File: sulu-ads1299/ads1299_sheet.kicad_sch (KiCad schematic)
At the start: 13 parts

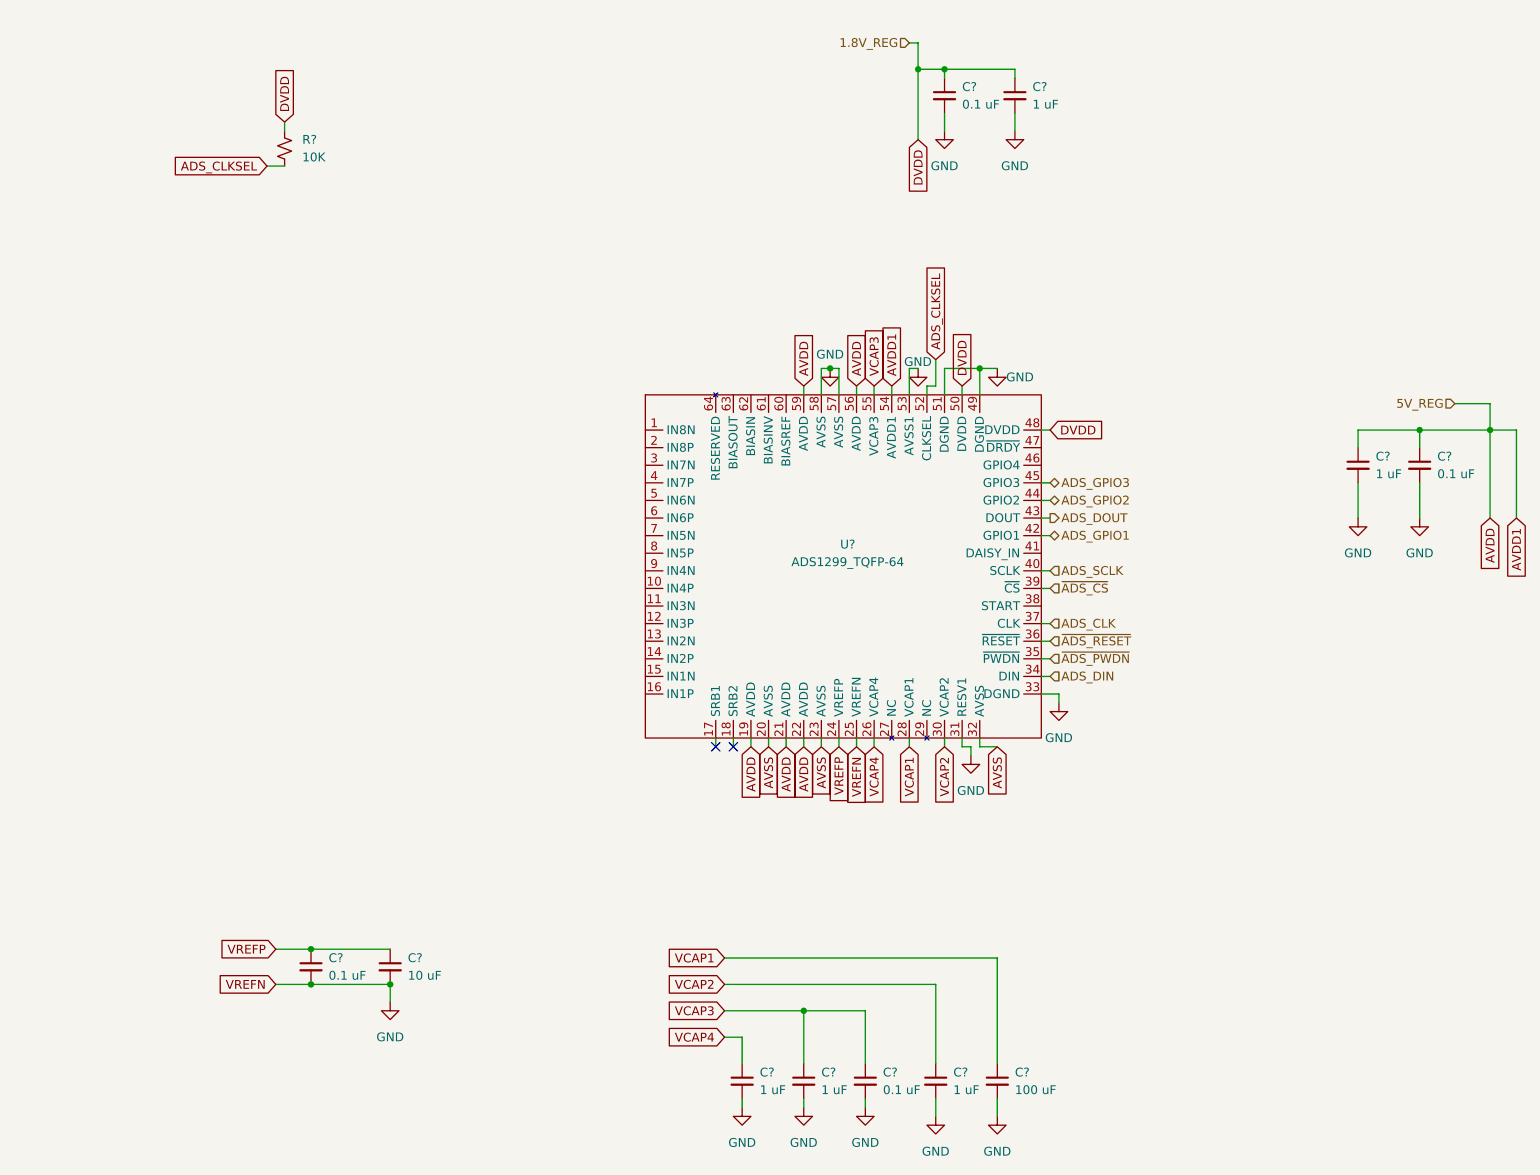
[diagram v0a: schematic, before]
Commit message: Sulu-ads1299 schematic largely completed
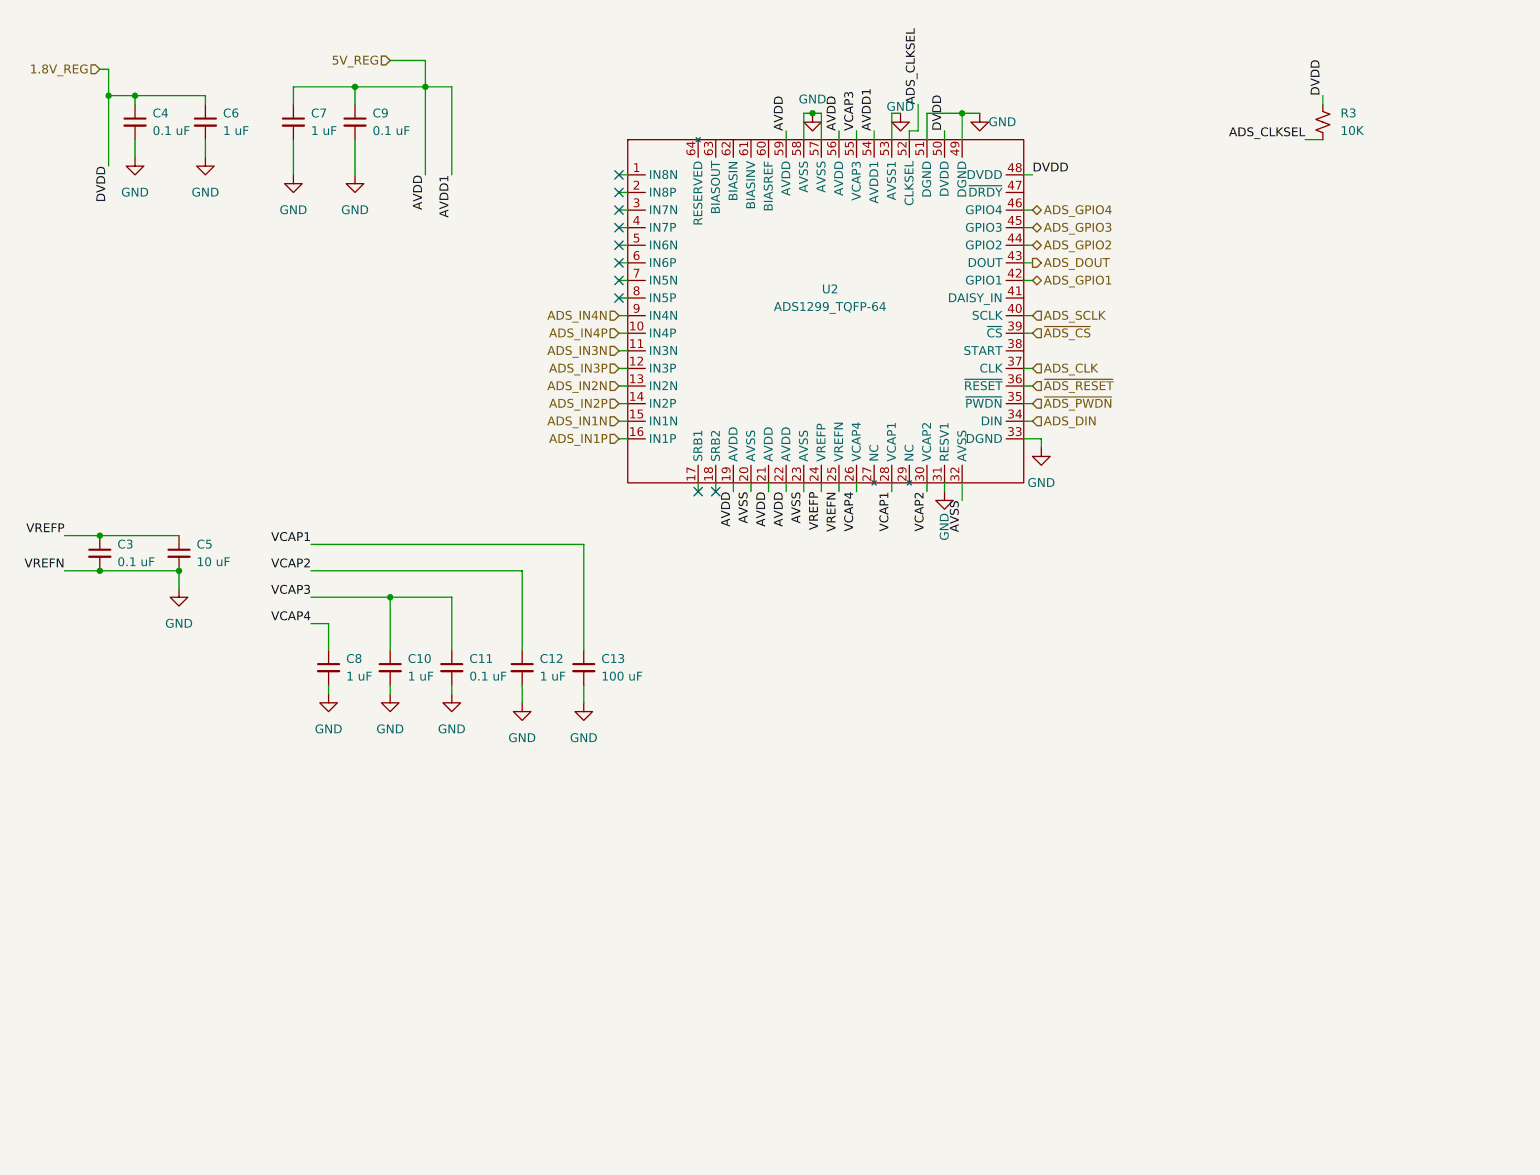
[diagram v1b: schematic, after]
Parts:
- gave numbers to parts that had none: 13
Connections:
- net ADS_IN4P: now reaches U2.10 (IN4P)
- net ADS_IN3N: now reaches U2.11 (IN3N)
- net ADS_IN3P: now reaches U2.12 (IN3P)
- net ADS_IN2N: now reaches U2.13 (IN2N)
- net ADS_IN2P: now reaches U2.14 (IN2P)
- net ADS_IN1N: now reaches U2.15 (IN1N)
- net ADS_IN1P: now reaches U2.16 (IN1P)
- net ADS_GPIO4: now reaches U2.46 (GPIO4)
- net ADS_IN4N: now reaches U2.9 (IN4N)
- net AVDD renamed 5V_REG
- net DVDD renamed 1.8V_REG
- no-connect marks 2 -> 10
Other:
- moved on the sheet: C10, C11, C12, C13, C3, C4, C5, C6, C7, C8, C9, R3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

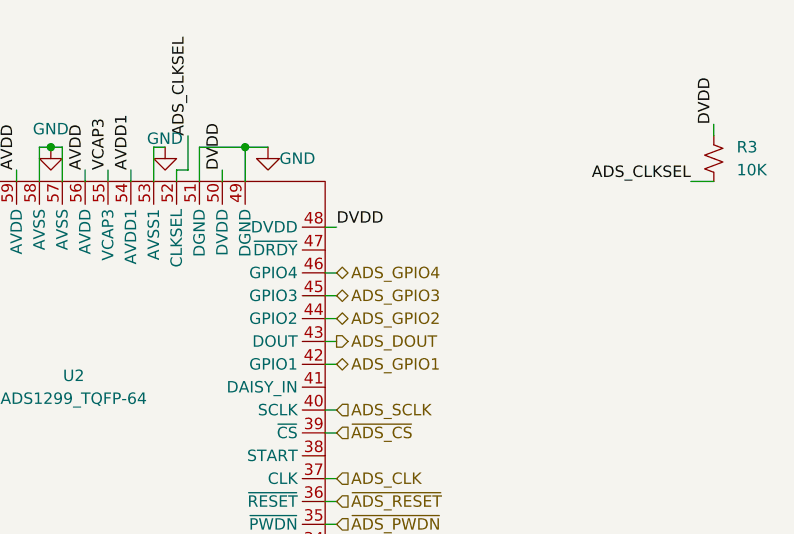
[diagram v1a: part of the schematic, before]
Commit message: Sulu-ads1299 migrating libs and fixing ERC
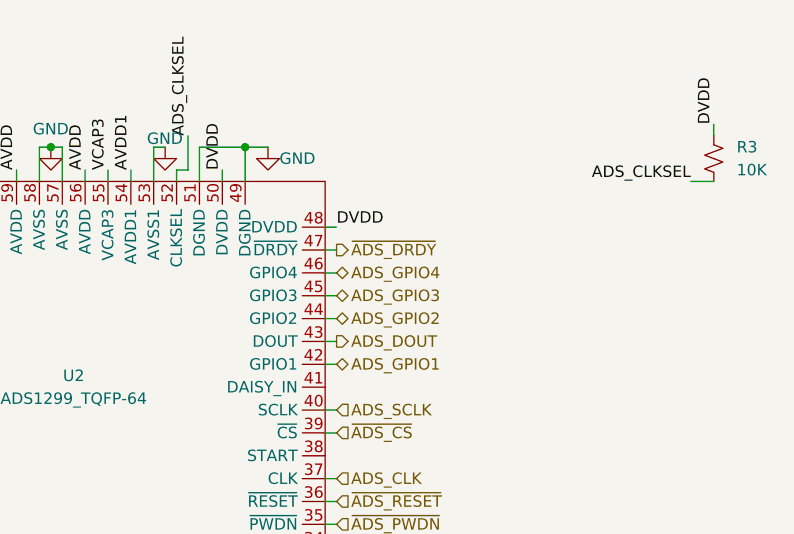
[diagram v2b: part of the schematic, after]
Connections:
- net ~{ADS_DRDY}: now reaches U2.47 (~{DRDY})
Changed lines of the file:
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@@
+    (stroke (width 0) (type default) (color 0 0 0 0))
+  )
+  (wire (pts (xy 162.56 43.18) (xy 163.83 43.18))
     (stroke (width 0) (type default) (color 0 0 0 0))
   )
@@
     (effects (font (size 1.27 1.27)) (justify left))
   )
+  (hierarchical_label "~{ADS_DRDY}" (shape output) (at 163.83 43.18 0)
+    (effects (font (size 1.27 1.27)) (justify left))
+  )

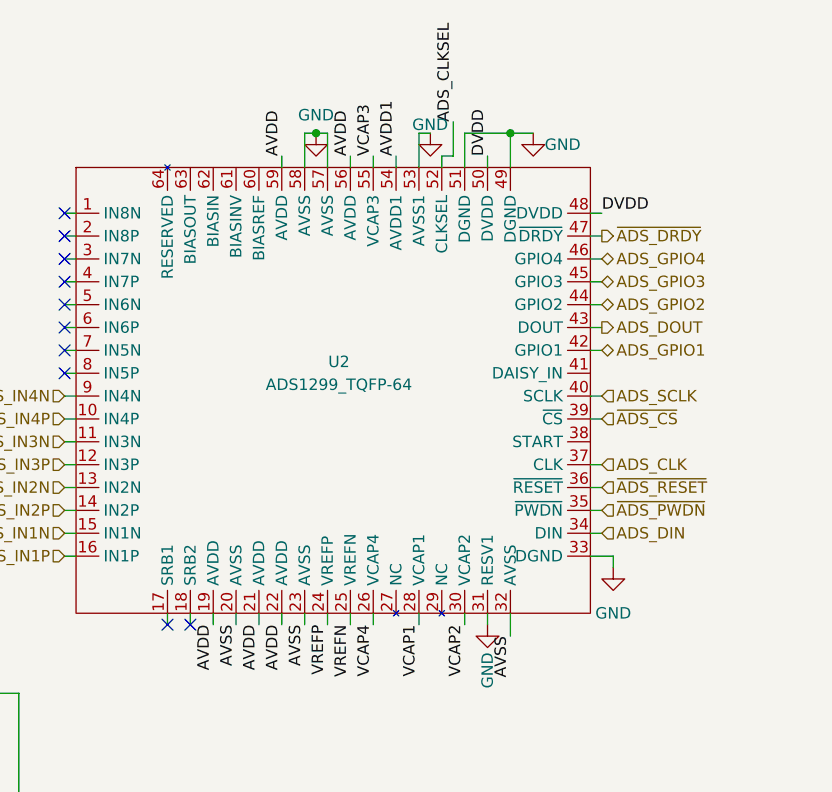
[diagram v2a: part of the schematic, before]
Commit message: Sulu-ads1299 started layout & imported shared footprints
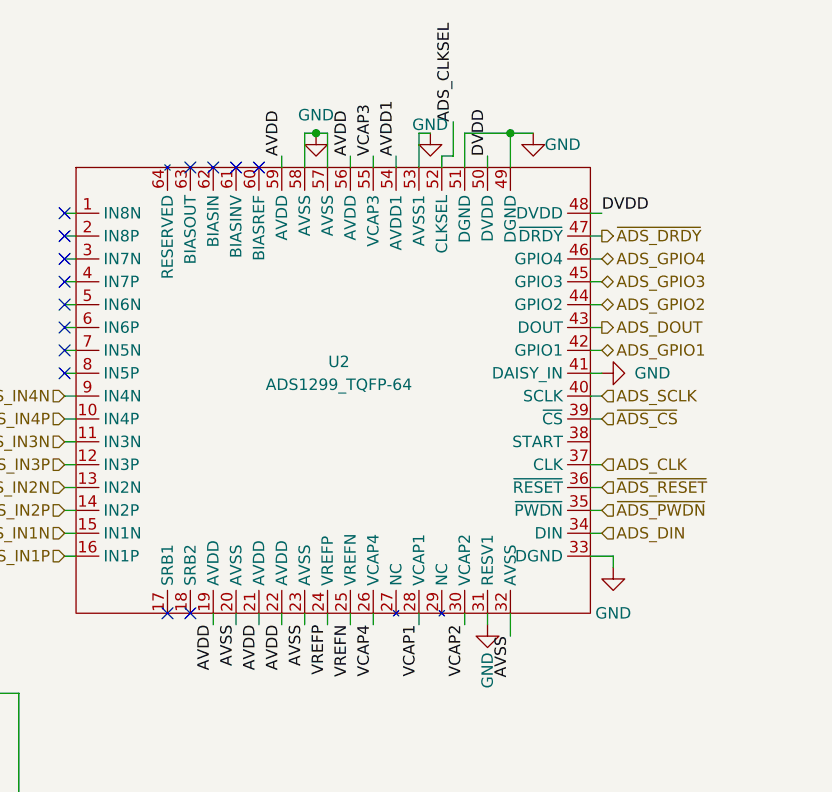
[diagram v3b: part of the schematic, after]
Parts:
- C10, C11, C3, C4, C5, C6, C7, C8, C9: footprint (none) -> Capacitor_SMD:C_0402_1005Metric
- R3: footprint (none) -> Resistor_SMD:R_0402_1005Metric
- U2: footprint (none) -> Package_QFP:TQFP-64_10x10mm_P0.5mm
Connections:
- net GND: now also U2.41 (DAISY_IN)
- no-connect marks 10 -> 14
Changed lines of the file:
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@@
   )
   (no_connect (at 104.14 48.26))
+  (no_connect (at 123.19 35.56))
+  (no_connect (at 118.11 85.09))
   (no_connect (at 104.14 40.64))
-  (no_connect (at 115.57 86.36))
+  (no_connect (at 120.65 35.56))
   (no_connect (at 104.14 50.8))
   (no_connect (at 104.14 45.72))
@@
   (no_connect (at 104.14 58.42))
   (no_connect (at 104.14 55.88))
-  (no_connect (at 118.11 86.36))
+  (no_connect (at 115.57 85.09))
+  (no_connect (at 118.11 35.56))
+  (no_connect (at 125.73 35.56))
   (no_connect (at 104.14 53.34))
   (wire (pts (xy 29.21 97.79) (xy 40.64 97.79))
@@
     (stroke (width 0) (type default) (color 0 0 0 0))
   )
-  (wire (pts (xy 115.57 86.36) (xy 115.57 85.09))
-    (stroke (width 0) (type default) (color 0 0 0 0))
-  )
   (wire (pts (xy 138.43 34.29) (xy 138.43 35.56))
     (stroke (width 0) (type default) (color 0 0 0 0))
@@
     (stroke (width 0) (type default) (color 0 0 0 0))
   )
+  (wire (pts (xy 162.56 58.42) (xy 163.83 58.42))
+    (stroke (width 0) (type default) (color 0 0 0 0))
+  )
   (wire (pts (xy 162.56 76.2) (xy 163.83 76.2))
     (stroke (width 0) (type default) (color 0 0 0 0))
@@
   )
   (wire (pts (xy 66.04 27.94) (xy 57.15 27.94))
-    (stroke (width 0) (type default) (color 0 0 0 0))
-  )
-  (wire (pts (xy 118.11 85.09) (xy 118.11 86.36))
     (stroke (width 0) (type default) (color 0 0 0 0))
   )
@@
       (effects (font (size 1.27 1.27)) (justify left))
     )
-    (property "Footprint" "" (id 2) (at 40.64 95.25 0)
+    (property "Footprint" "Capacitor_SMD:C_0402_1005Metric" (id 2) (at 40.64 95.25 0)
       (effects (font (size 1.27 1.27)) hide)
     )
@@
     (property "Reference" "U2" (id 0) (at 134.62 57.15 0))
     (property "Value" "ADS1299_TQFP-64" (id 1) (at 134.62 59.69 0))
-    (property "Footprint" "" (id 2) (at 77.47 54.61 0)
+    (property "Footprint" "Package_QFP:TQFP-64_10x10mm_P0.5mm" (id 2) (at 77.47 54.61 0)
       (effects (font (size 1.27 1.27)) hide)
     )
@@
       (effects (font (size 1.27 1.27)) (justify left))
     )
-    (property "Footprint" "" (id 2) (at 57.15 33.02 0)
+    (property "Footprint" "Capacitor_SMD:C_0402_1005Metric" (id 2) (at 57.15 33.02 0)
       (effects (font (size 1.27 1.27)) hide)
     )
@@
       (effects (font (size 1.27 1.27)) (justify left))
     )
-    (property "Footprint" "" (id 2) (at 44.45 33.02 0)
+    (property "Footprint" "Capacitor_SMD:C_0402_1005Metric" (id 2) (at 44.45 33.02 0)
       (effects (font (size 1.27 1.27)) hide)
     )
@@
       (effects (font (size 1.27 1.27)) (justify left))
     )
-    (property "Footprint" "" (id 2) (at 62.23 111.76 0)
+    (property "Footprint" "Capacitor_SMD:C_0402_1005Metric" (id 2) (at 62.23 111.76 0)
       (effects (font (size 1.27 1.27)) hide)
     )
@@
       (effects (font (size 1.27 1.27)) (justify left))
     )
-    (property "Footprint" "" (id 2) (at 66.04 33.02 0)
+    (property "Footprint" "Capacitor_SMD:C_0402_1005Metric" (id 2) (at 66.04 33.02 0)
       (effects (font (size 1.27 1.27)) hide)
     )
@@
       (effects (font (size 1.27 1.27)) (justify left))
     )
-    (property "Footprint" "" (id 2) (at 29.21 95.25 0)
+    (property "Footprint" "Capacitor_SMD:C_0402_1005Metric" (id 2) (at 29.21 95.25 0)
       (effects (font (size 1.27 1.27)) hide)
     )
@@
       (effects (font (size 1.27 1.27)) (justify left))
     )
-    (property "Footprint" "" (id 2) (at 71.12 111.76 0)
+    (property "Footprint" "Capacitor_SMD:C_0402_1005Metric" (id 2) (at 71.12 111.76 0)
       (effects (font (size 1.27 1.27)) hide)
     )
@@
       (effects (font (size 1.27 1.27)) (justify left))
     )
-    (property "Footprint" "" (id 2) (at 205.74 33.02 0)
+    (property "Footprint" "Resistor_SMD:R_0402_1005Metric" (id 2) (at 205.74 33.02 0)
       (effects (font (size 1.27 1.27)) hide)
     )
@@
       (effects (font (size 1.27 1.27)) (justify left))
     )
-    (property "Footprint" "" (id 2) (at 34.29 33.02 0)
+    (property "Footprint" "Capacitor_SMD:C_0402_1005Metric" (id 2) (at 34.29 33.02 0)
       (effects (font (size 1.27 1.27)) hide)
     )
@@
       (effects (font (size 1.27 1.27)) (justify left))
     )
-    (property "Footprint" "" (id 2) (at 80.01 111.76 0)
+    (property "Footprint" "Capacitor_SMD:C_0402_1005Metric" (id 2) (at 80.01 111.76 0)
       (effects (font (size 1.27 1.27)) hide)
     )
@@
     (pin "2")
   )
+  (symbol (lib_id "power:GND") (at 163.83 58.42 90) (unit 1)
+    (in_bom yes) (on_board yes)
+    (property "Reference" "#PWR0115" (id 0) (at 170.18 58.42 0)
+      (effects (font (size 1.27 1.27)) hide)
+    )
+    (property "Value" "GND" (id 1) (at 171.45 58.42 90)
+      (effects (font (size 1.27 1.27)) (justify left))
+    )
+    (property "Footprint" "" (id 2) (at 163.83 58.42 0)
+      (effects (font (size 1.27 1.27)) hide)
+    )
+    (property "Datasheet" "" (id 3) (at 163.83 58.42 0)
+      (effects (font (size 1.27 1.27)) hide)
+    )
+    (pin "1")
+  )
   (symbol (lib_id "power:GND") (at 144.78 31.75 0) (unit 1)
